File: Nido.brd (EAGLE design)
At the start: 26.2 x 16 mm, 9 parts, among them J1 2X6 FEMALE, K1 HE3621, T1 BC337, U1 BME280

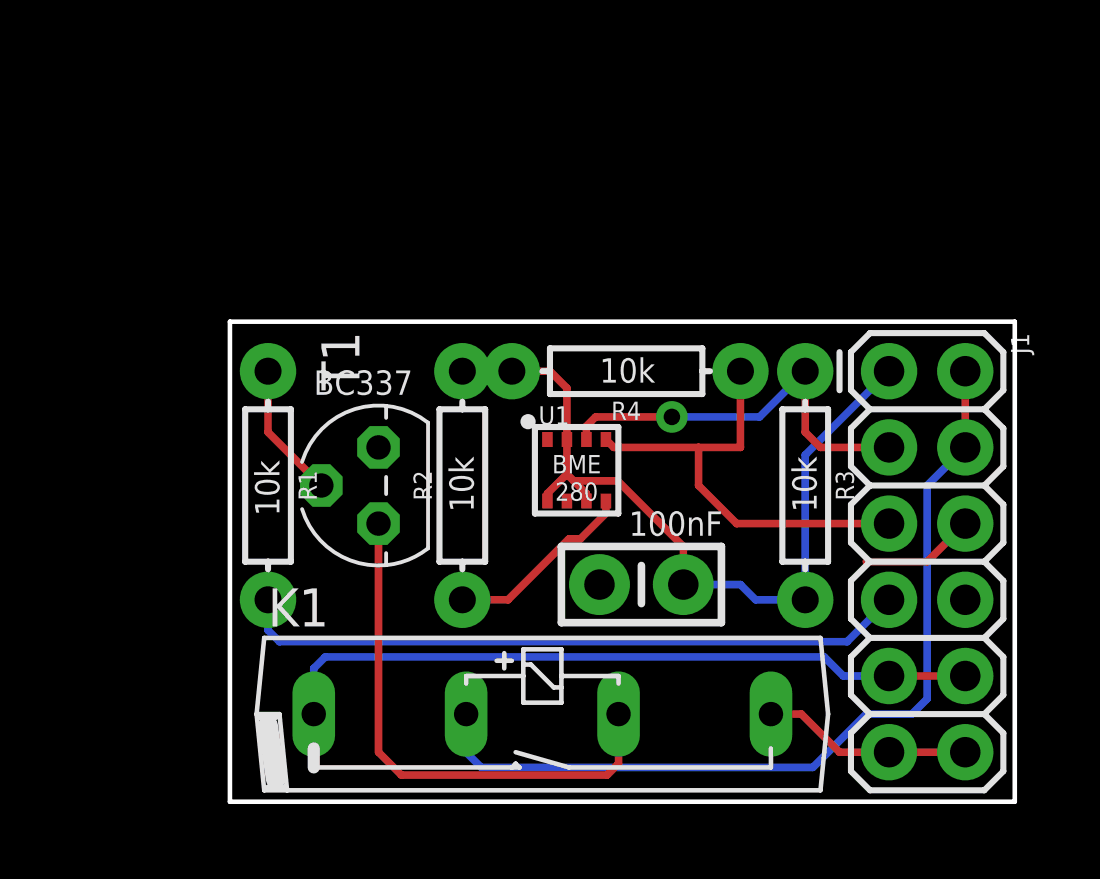
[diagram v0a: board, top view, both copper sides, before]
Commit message: Updated board components, added PCB photos
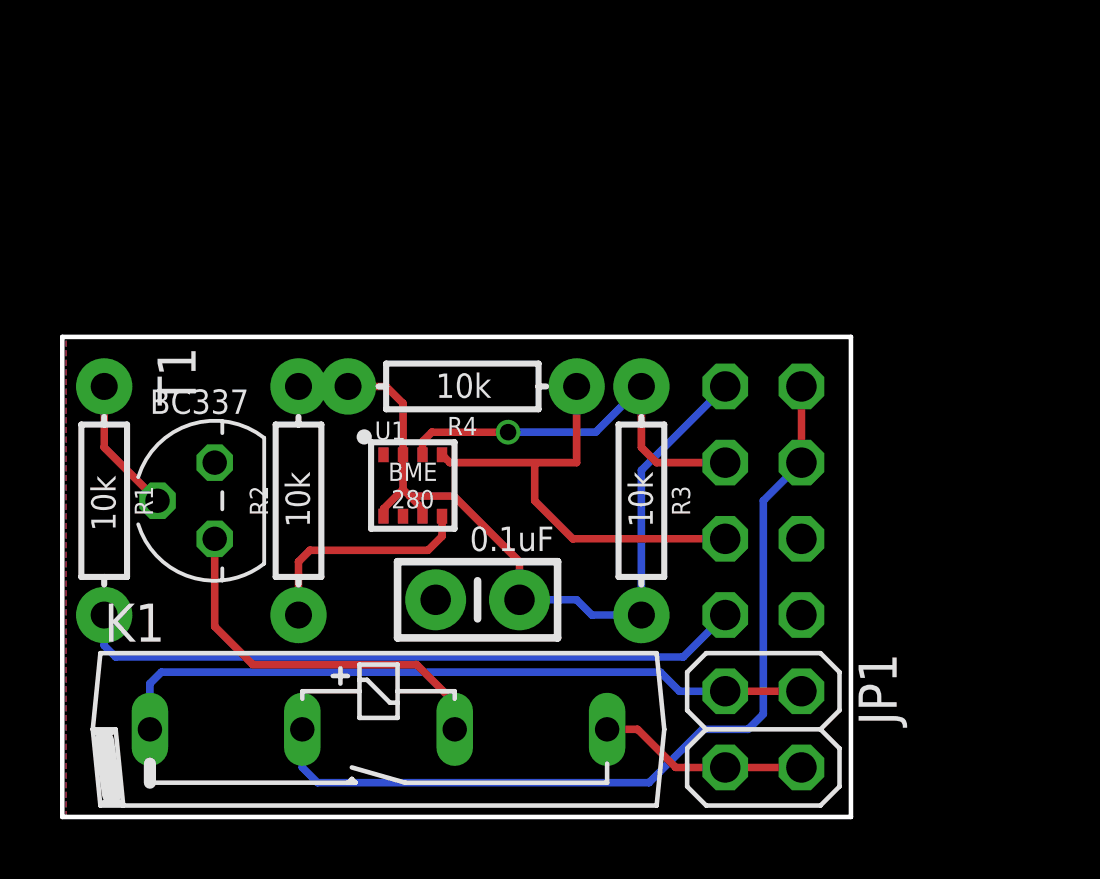
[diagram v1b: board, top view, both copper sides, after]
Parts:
- removed J1: 2X6 FEMALE, SparkFun-Connectors:2X6
- added JP1: (no value), pinhead:2X02
- added JP2: (no value), pinhead:2X04
- moved R3 5.48 mm to (19.2, 10.5)
- moved C1 5.48 mm to (13.7, 7.24)
- moved K1 5.48 mm to (10.4, 2.92)
- moved R1 5.48 mm to (1.27, 10.5)
- moved R2 5.48 mm to (7.75, 10.5)
- moved R4 5.48 mm to (13.2, 14.4)
- moved U1 5.48 mm to (11.6, 11.0)
- moved T1 5.48 mm to (4.95, 10.5)
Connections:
- net 3V3: now also JP2.2; no longer J1.1
- net 5V: now also JP2.1, JP2.3; no longer J1.2, J1.4
- net GND: now also JP2.5; no longer J1.6
- net GPIO_14: now also JP2.7; no longer J1.8
- net GPIO_4: now also JP2.8; no longer J1.7
- net HEATER1: now also JP1.1, JP1.2; no longer J1.10, J1.9
- net HEATER2: now also JP1.3, JP1.4; no longer J1.11, J1.12
- net SCL: now also JP2.6; no longer J1.5
- net SDA: now also JP2.4; no longer J1.3
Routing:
- net N$5: track 17.7 -> 12.9 mm
- net GND: track 3.83 -> 0.00 mm
- net N$1: track 6.39 -> 7.58 mm
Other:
- board size 26.2 x 16 mm -> 26.3 x 16 mm
- board text added: "0.1uF"
- board text added: "Nido v1.0"
- board text added: "https://github.com/alexmensch/nido"
- board text removed: "100nF"

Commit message: Updated Nido PCB v2 files
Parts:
- removed C1: 0.1uF, SparkFun-Capacitors:CAP-PTH-SMALL-KIT
- removed K1: HE3621, relay:HE3621
- removed R4: 10k, SparkFun-Resistors:AXIAL-0.3
- removed T1: BC337, transistor:TO92
- added C2: 0.1uF, SparkFun-Capacitors:0402
- added Q1: 500mA/300V, SparkFun-DiscreteSemi:SOT23-3
- added R5: 10k, SparkFun-Resistors:0402
- added U2: CPC1017NSOP4, nido:CPC1017N
- JP1: value (none) -> 1986712-2TH; device pinhead:2X02 -> nido:1986712-2
- R1, R2, R3: device SparkFun-Resistors:AXIAL-0.3 -> SparkFun-Resistors:0402
- moved JP1 14.8 mm to (8.76, 5.97), turned to 90 degrees
- moved JP2 11.6 mm to (13.5, 16.8)
- moved R1 11.4 mm to (8.38, 19.4), turned to 180 degrees
- moved R3 11.2 mm to (8.00, 10.7), flipped to the bottom, turned to 180 degrees
- moved R2 7.68 mm to (9.91, 17.9), flipped to the bottom
- moved U1 6.21 mm to (8.38, 16.4)
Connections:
- net 3V3: now also C2.1, R1.2, R2.2, R5.2; no longer C1.1, R2.P$2, R3.P$2, R4.P$2
- net 5V: now also U2.1; no longer K1.2
- net GND: now also C2.2, Q1.2; no longer C1.2, T1.1
- net GPIO_4: now also R3.2; no longer R1.P$2
- net HEATER1: now also JP1.P$1, JP1.P$2, U2.4; no longer JP1.1, JP1.2, K1.1
- net HEATER2: now also JP1.P$3, JP1.P$4, U2.3; no longer JP1.3, JP1.4, K1.4
- net N$1: now also R5.1; no longer R2.P$1
- net N$5: now also Q1.3, U2.2; no longer K1.3, T1.3
- net N$6: now also Q1.1, R3.1; no longer R1.P$1, T1.2
- net SCL: now also R2.1; no longer R4.P$1
- net SDA: now also R1.1; no longer R3.P$1
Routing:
- net GND: track 0.00 -> 26.3 mm
- net GPIO_4: track 22.5 -> 4.56 mm
- net 5V: track 29.2 -> 18.7 mm
- net SCL: track 15.3 -> 7.52 mm
- net SDA: track 13.5 -> 5.94 mm, vias 1 -> 0
- net N$1: track 7.58 -> 2.19 mm
- net N$5: track 12.9 -> 8.01 mm
- net 3V3: track 27.8 -> 25.1 mm
- net N$6: track 4.55 -> 2.73 mm
- net HEATER2: track 7.00 -> 8.68 mm
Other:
- board size 26.3 x 16 mm -> 13.3 x 21.5 mm
- board text added: "Nido v2"
- board text removed: "0.1uF"
- board text removed: "10k"
- board text removed: "BC337"
- board text removed: "BME 280"
- board text removed: "Nido v1.0"
- board text removed: "https://github.com/alexmensch/nido"
